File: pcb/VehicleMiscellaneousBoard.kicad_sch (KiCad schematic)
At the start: 13 parts, among them J2 Conn_02x05_Top_Bottom, J4 B8B-XH-A, U1 OpenMV H7+, U2 Seeed_Studio_XIAO-ESP32-S3-Se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

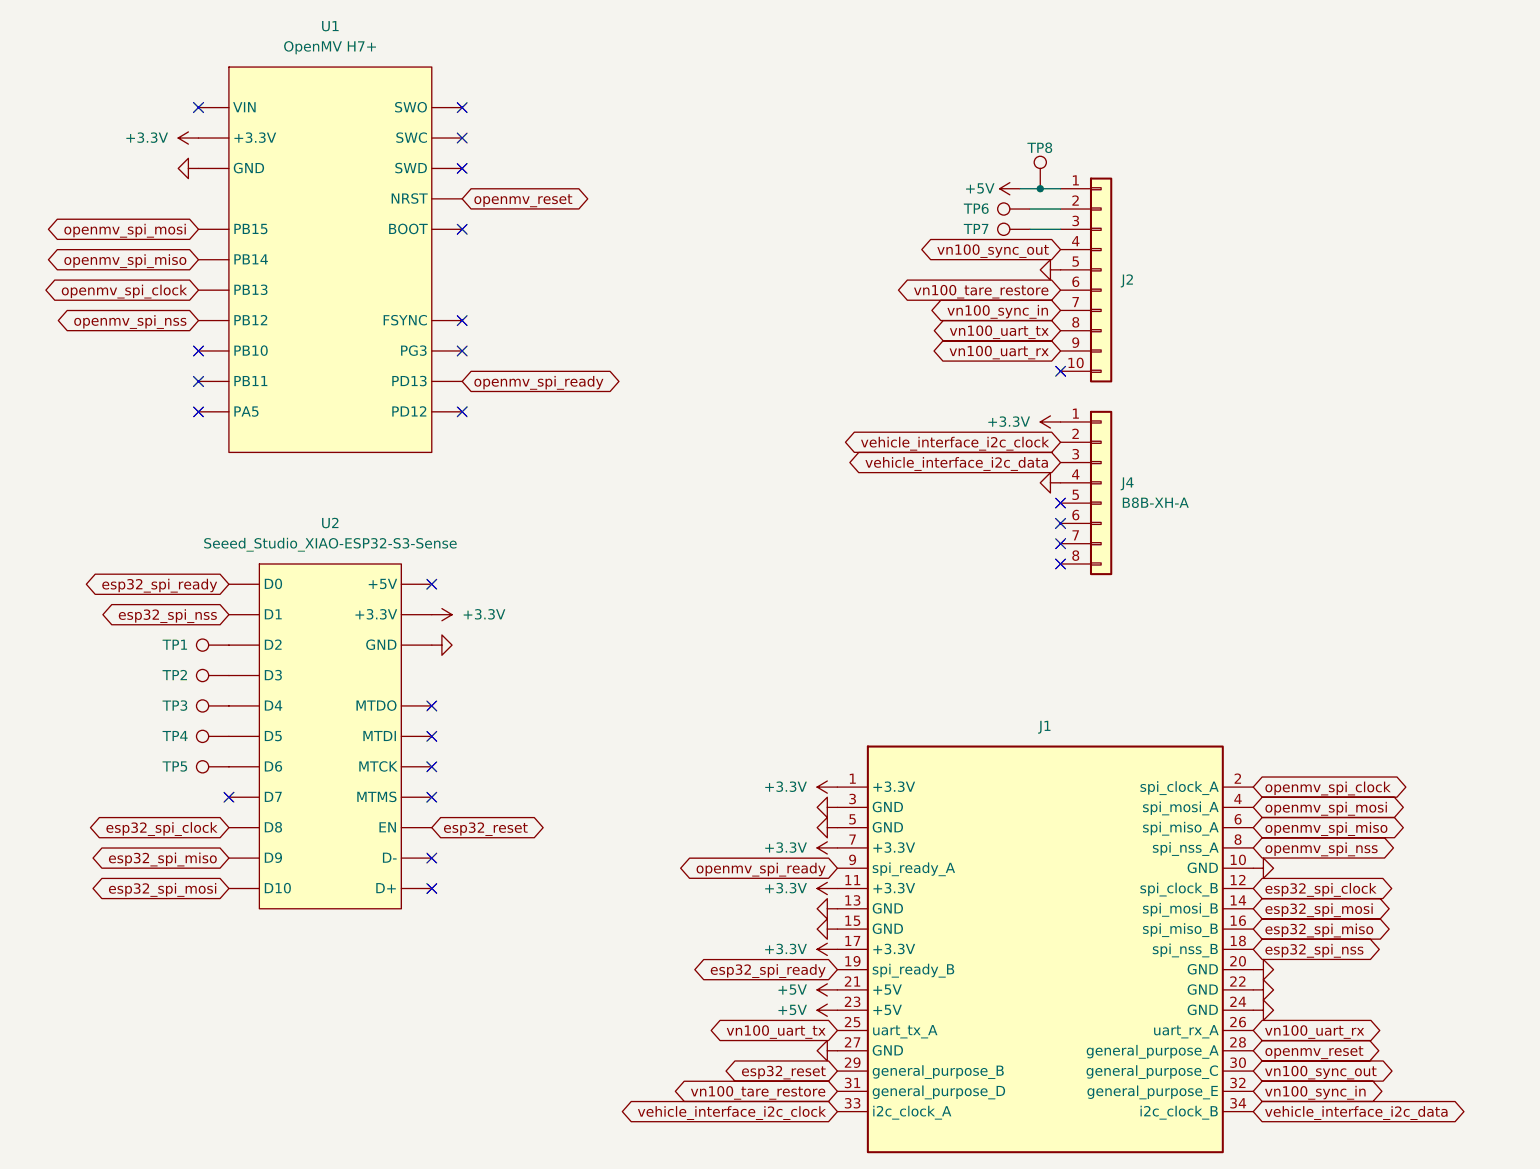
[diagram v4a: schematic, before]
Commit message: Deprecated ESP32 SPI pins for `VehicleFlightComputer` and `VehicleMiscellaneousBoard`.
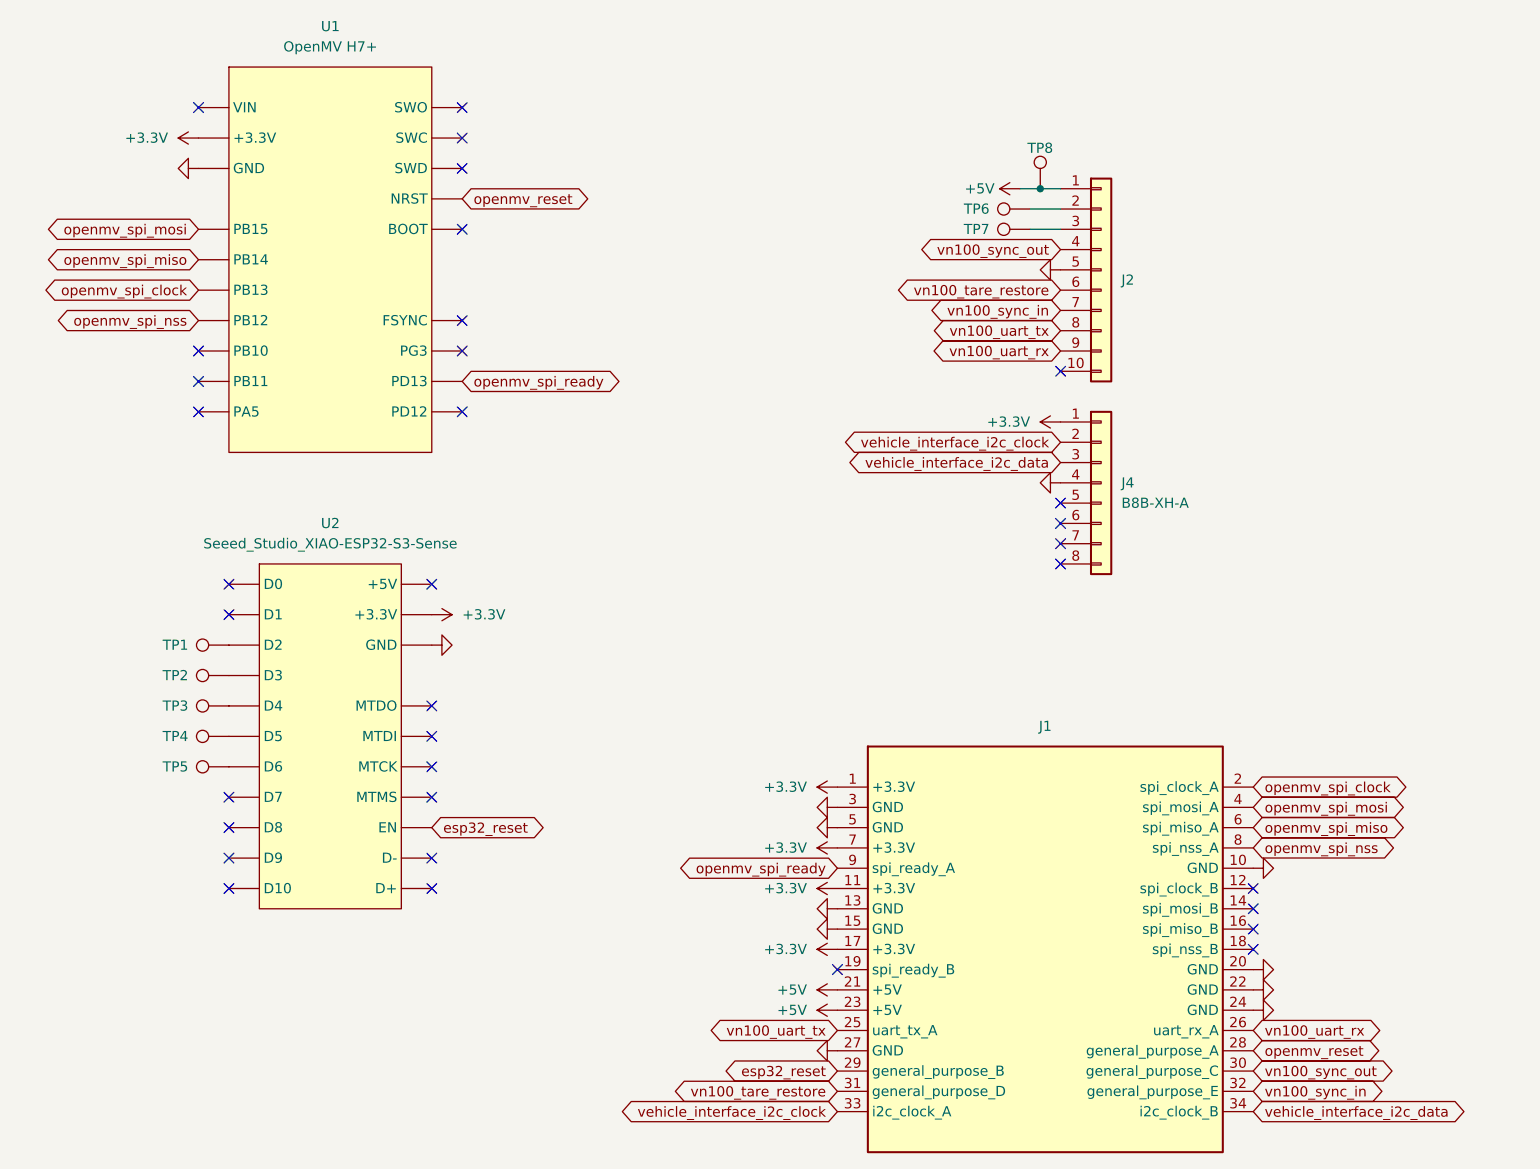
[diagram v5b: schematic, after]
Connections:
- net esp32_spi_clock: no longer names the net of J1.12 (spi_clock_B)
- net esp32_spi_clock: no longer U2.D8
- net esp32_spi_miso: no longer names the net of J1.16 (spi_miso_B)
- net esp32_spi_miso: no longer U2.D9
- net esp32_spi_mosi: no longer names the net of J1.14 (spi_mosi_B)
- net esp32_spi_mosi: no longer U2.D10
- net esp32_spi_nss: no longer names the net of J1.18 (spi_nss_B)
- net esp32_spi_nss: no longer U2.D1
- net esp32_spi_ready: no longer names the net of J1.19 (spi_ready_B)
- net esp32_spi_ready: no longer U2.D0
- no-connect marks 24 -> 34
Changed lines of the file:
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@@
+	)
+	(no_connect
+		(at 224.79 158.75)
 	)
 	(no_connect
@@
 	)
 	(no_connect
+		(at 96.52 115.57)
+	)
+	(no_connect
 		(at 125.73 82.55)
 	)
@@
 	)
 	(no_connect
+		(at 96.52 119.38)
+	)
+	(no_connect
 		(at 125.73 86.36)
 	)
@@
 	)
 	(no_connect
+		(at 96.52 149.86)
+	)
+	(no_connect
+		(at 96.52 153.67)
+	)
+	(no_connect
 		(at 121.92 153.67)
 	)
@@
 	)
 	(no_connect
+		(at 224.79 161.29)
+	)
+	(no_connect
 		(at 200.66 107.95)
 	)
@@
 	)
 	(no_connect
+		(at 172.72 163.83)
+	)
+	(no_connect
 		(at 121.92 115.57)
 	)
@@
 	)
 	(no_connect
+		(at 224.79 156.21)
+	)
+	(no_connect
 		(at 92.71 90.17)
 	)
 	(no_connect
 		(at 125.73 59.69)
+	)
+	(no_connect
+		(at 96.52 146.05)
+	)
+	(no_connect
+		(at 224.79 153.67)
 	)
 	(no_connect
@@
 		)
 	)
-	(global_label "esp32_spi_clock"
-		(shape bidirectional)
-		(at 96.52 146.05 180)
-		(fields_autoplaced yes)
-		(effects
-			(font
-				(size 1.27 1.27)
-			)
-			(justify right)
-		)
-		(property "Intersheetrefs" "${INTERSHEET_REFS}"
-			(at 77.0022 146.05 0)
-			(effects
-				(font
-					(size 1.27 1.27)
-				)
-				(justify right)
-				(hide yes)
-			)
-		)
-	)
 	(global_label "vn100_uart_rx"
 		(shape bidirectional)
@@
 		)
 	)
-	(global_label "esp32_spi_nss"
-		(shape bidirectional)
-		(at 224.79 161.29 0)
-		(fields_autoplaced yes)
-		(effects
-			(font
-				(size 1.27 1.27)
-			)
-			(justify left)
-		)
-		(property "Intersheetrefs" "${INTERSHEET_REFS}"
-			(at 242.4935 161.29 0)
-			(effects
-				(font
-					(size 1.27 1.27)
-				)
-				(justify left)
-				(hide yes)
-			)
-		)
-	)
 	(global_label "vn100_sync_in"
 		(shape bidirectional)
@@
 		)
 	)
-	(global_label "esp32_spi_ready"
-		(shape bidirectional)
-		(at 96.52 115.57 180)
-		(fields_autoplaced yes)
-		(effects
-			(font
-				(size 1.27 1.27)
-			)
-			(justify right)
-		)
-		(property "Intersheetrefs" "${INTERSHEET_REFS}"
-			(at 76.8813 115.57 0)
-			(effects
-				(font
-					(size 1.27 1.27)
-				)
-				(justify right)
-				(hide yes)
-			)
-		)
-	)
 	(global_label "vn100_uart_tx"
 		(shape bidirectional)
@@
 		)
 	)
-	(global_label "esp32_spi_miso"
-		(shape bidirectional)
-		(at 224.79 158.75 0)
-		(fields_autoplaced yes)
-		(effects
-			(font
-				(size 1.27 1.27)
-			)
-			(justify left)
-		)
-		(property "Intersheetrefs" "${INTERSHEET_REFS}"
-			(at 243.7635 158.75 0)
-			(effects
-				(font
-					(size 1.27 1.27)
-				)
-				(justify left)
-				(hide yes)
-			)
-		)
-	)
 	(global_label "openmv_spi_clock"
 		(shape bidirectional)
@@
 		)
 	)
-	(global_label "esp32_spi_mosi"
-		(shape bidirectional)
-		(at 96.52 153.67 180)
-		(fields_autoplaced yes)
-		(effects
-			(font
-				(size 1.27 1.27)
-			)
-			(justify right)
-		)
-		(property "Intersheetrefs" "${INTERSHEET_REFS}"
-			(at 77.5465 153.67 0)
-			(effects
-				(font
-					(size 1.27 1.27)
-				)
-				(justify right)
-				(hide yes)
-			)
-		)
-	)
 	(global_label "esp32_reset"
 		(shape bidirectional)
@@
 		)
 	)
-	(global_label "esp32_spi_mosi"
-		(shape bidirectional)
-		(at 224.79 156.21 0)
-		(fields_autoplaced yes)
-		(effects
-			(font
-				(size 1.27 1.27)
-			)
-			(justify left)
-		)
-		(property "Intersheetrefs" "${INTERSHEET_REFS}"
-			(at 243.7635 156.21 0)
-			(effects
-				(font
-					(size 1.27 1.27)
-				)
-				(justify left)
-				(hide yes)
-			)
-		)
-	)
-	(global_label "esp32_spi_miso"
-		(shape bidirectional)
-		(at 96.52 149.86 180)
-		(fields_autoplaced yes)
-		(effects
-			(font
-				(size 1.27 1.27)
-			)
-			(justify right)
-		)
-		(property "Intersheetrefs" "${INTERSHEET_REFS}"
-			(at 77.5465 149.86 0)
-			(effects
-				(font
-					(size 1.27 1.27)
-				)
-				(justify right)
-				(hide yes)
-			)
-		)
-	)
-	(global_label "esp32_spi_clock"
-		(shape bidirectional)
-		(at 224.79 153.67 0)
-		(fields_autoplaced yes)
-		(effects
-			(font
-				(size 1.27 1.27)
-			)
-			(justify left)
-		)
-		(property "Intersheetrefs" "${INTERSHEET_REFS}"
-			(at 244.3078 153.67 0)
-			(effects
-				(font
-					(size 1.27 1.27)
-				)
-				(justify left)
-				(hide yes)
-			)
-		)
-	)
 	(global_label "vn100_tare_restore"
 		(shape bidirectional)
@@
 		)
 	)
-	(global_label "esp32_spi_ready"
-		(shape bidirectional)
-		(at 172.72 163.83 180)
-		(fields_autoplaced yes)
-		(effects
-			(font
-				(size 1.27 1.27)
-			)
-			(justify right)
-		)
-		(property "Intersheetrefs" "${INTERSHEET_REFS}"
-			(at 153.0813 163.83 0)
-			(effects
-				(font
-					(size 1.27 1.27)
-				)
-				(justify right)
-				(hide yes)
-			)
-		)
-	)
 	(global_label "vehicle_interface_i2c_clock"
 		(shape bidirectional)
@@
 				(hide yes)
 			)
-		)
-	)
-	(global_label "esp32_spi_nss"
-		(shape bidirectional)
-		(at 96.52 119.38 180)
-		(fields_autoplaced yes)
-		(effects
-			(font
-				(size 1.27 1.27)
-			)
-			(justify right)
-		)
-		(property "Intersheetrefs" "${INTERSHEET_REFS}"
-			(at 78.8165 119.38 0)
-			(effects
-				(font
-					(size 1.27 1.27)
-				)
-				(justify right)
-				(hide yes)
-			)

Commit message: Deprecated `vn100_tare_restore`, `vn100_sync_out`, and `vn100_sync_in` for `VehicleFlightComputer` and `VehicleMiscellaneousBoard`.
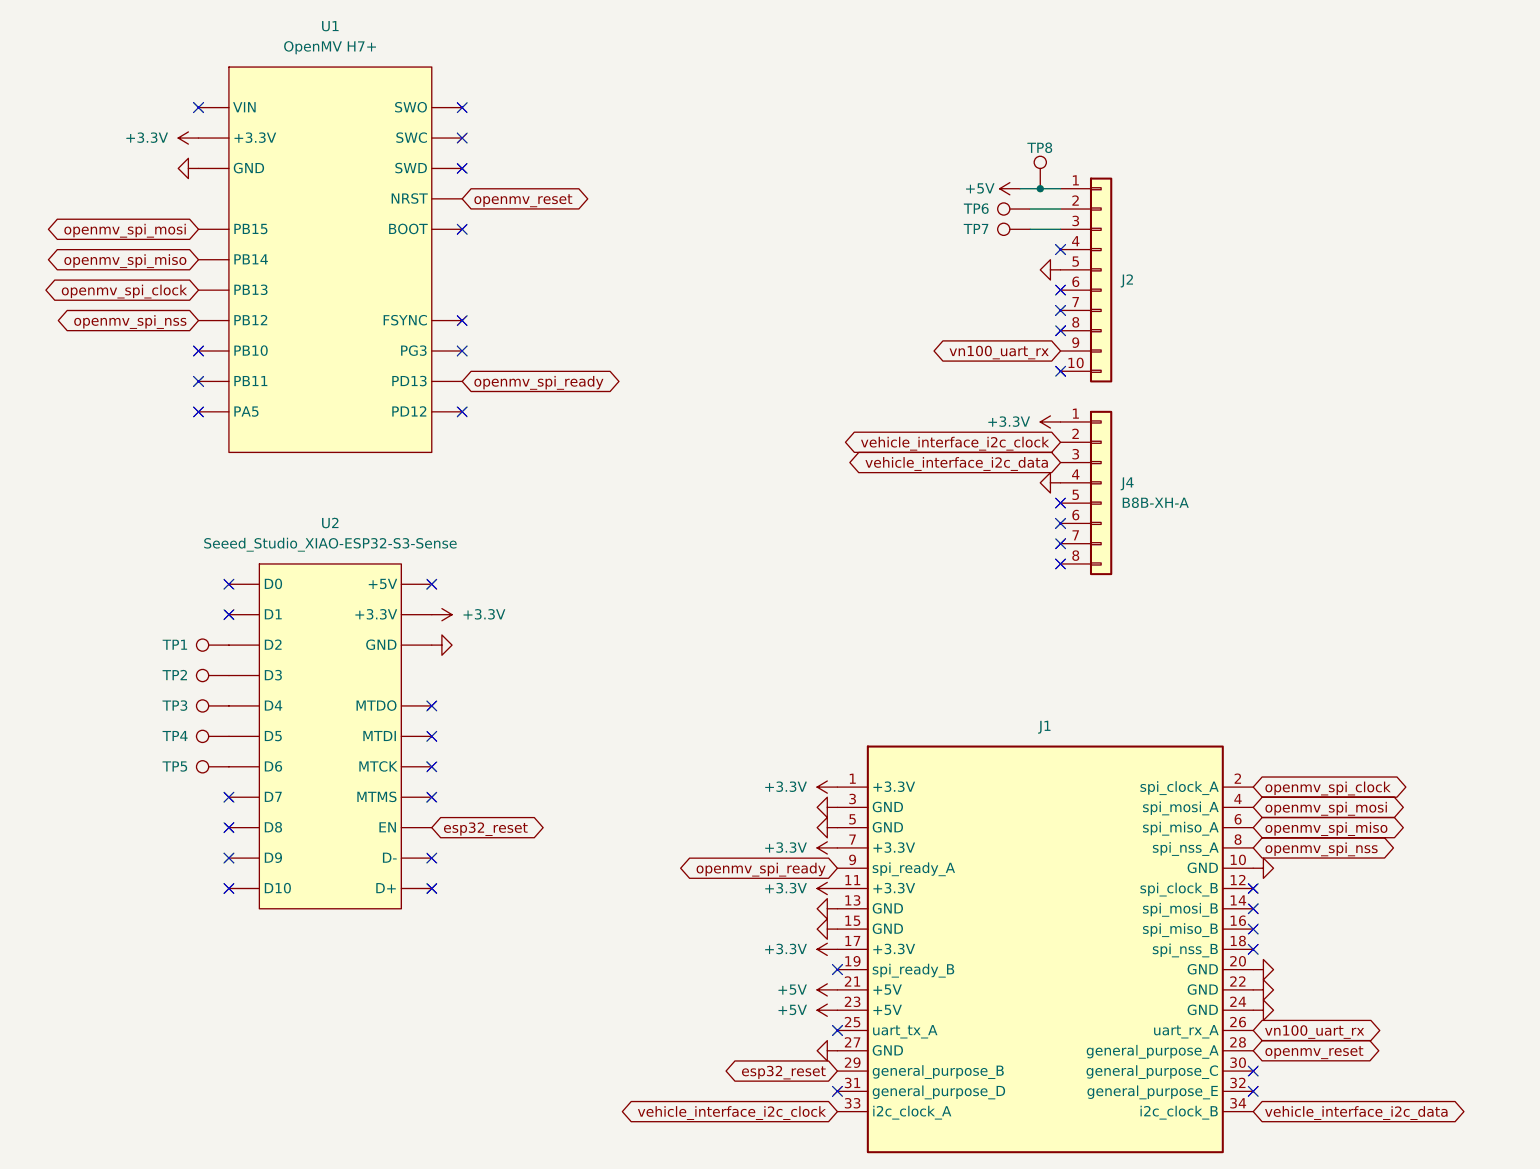
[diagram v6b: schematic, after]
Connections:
- net vn100_sync_in: no longer names the net of J1.32 (general_purpose_E)
- net vn100_sync_in: no longer J2.7 (Pin_7)
- net vn100_sync_out: no longer names the net of J1.30 (general_purpose_C)
- net vn100_sync_out: no longer J2.4 (Pin_4)
- net vn100_tare_restore: no longer names the net of J1.31 (general_purpose_D)
- net vn100_tare_restore: no longer J2.6 (Pin_6)
- net vn100_uart_tx: no longer names the net of J1.25 (uart_tx_A)
- net vn100_uart_tx: no longer J2.8 (Pin_8)
- no-connect marks 34 -> 42
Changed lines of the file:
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@@
+	)
+	(no_connect
+		(at 200.66 78.74)
 	)
 	(no_connect
@@
 	)
 	(no_connect
+		(at 200.66 83.82)
+	)
+	(no_connect
+		(at 200.66 81.28)
+	)
+	(no_connect
 		(at 92.71 55.88)
 	)
@@
 	)
 	(no_connect
+		(at 172.72 171.45)
+	)
+	(no_connect
 		(at 200.66 88.9)
 	)
 	(no_connect
+		(at 224.79 176.53)
+	)
+	(no_connect
 		(at 96.52 149.86)
 	)
@@
 	)
 	(no_connect
+		(at 224.79 179.07)
+	)
+	(no_connect
 		(at 200.66 107.95)
 	)
@@
 	(no_connect
 		(at 96.52 146.05)
+	)
+	(no_connect
+		(at 172.72 179.07)
+	)
+	(no_connect
+		(at 200.66 73.66)
 	)
 	(no_connect
@@
 		)
 	)
-	(global_label "vn100_uart_tx"
-		(shape bidirectional)
-		(at 172.72 171.45 180)
-		(fields_autoplaced yes)
-		(effects
-			(font
-				(size 1.27 1.27)
-			)
-			(justify right)
-		)
-		(property "Intersheetrefs" "${INTERSHEET_REFS}"
-			(at 155.3795 171.45 0)
-			(effects
-				(font
-					(size 1.27 1.27)
-				)
-				(justify right)
-				(hide yes)
-			)
-		)
-	)
 	(global_label "vehicle_interface_i2c_data"
 		(shape bidirectional)
@@
 		)
 	)
-	(global_label "vn100_sync_in"
-		(shape bidirectional)
-		(at 200.66 81.28 180)
-		(fields_autoplaced yes)
-		(effects
-			(font
-				(size 1.27 1.27)
-			)
-			(justify right)
-		)
-		(property "Intersheetrefs" "${INTERSHEET_REFS}"
-			(at 182.8961 81.28 0)
-			(effects
-				(font
-					(size 1.27 1.27)
-				)
-				(justify right)
-				(hide yes)
-			)
-		)
-	)
 	(global_label "openmv_reset"
 		(shape bidirectional)
@@
 		)
 	)
-	(global_label "vn100_uart_tx"
-		(shape bidirectional)
-		(at 200.66 83.82 180)
-		(fields_autoplaced yes)
-		(effects
-			(font
-				(size 1.27 1.27)
-			)
-			(justify right)
-		)
-		(property "Intersheetrefs" "${INTERSHEET_REFS}"
-			(at 183.3195 83.82 0)
-			(effects
-				(font
-					(size 1.27 1.27)
-				)
-				(justify right)
-				(hide yes)
-			)
-		)
-	)
 	(global_label "esp32_reset"
 		(shape bidirectional)
@@
 		)
 	)
-	(global_label "vn100_tare_restore"
-		(shape bidirectional)
-		(at 200.66 78.74 180)
-		(fields_autoplaced yes)
-		(effects
-			(font
-				(size 1.27 1.27)
-			)
-			(justify right)
-		)
-		(property "Intersheetrefs" "${INTERSHEET_REFS}"
-			(at 178.4813 78.74 0)
-			(effects
-				(font
-					(size 1.27 1.27)
-				)
-				(justify right)
-				(hide yes)
-			)
-		)
-	)
 	(global_label "vehicle_interface_i2c_clock"
 		(shape bidirectional)
@@
 		)
 	)
-	(global_label "vn100_sync_in"
-		(shape bidirectional)
-		(at 224.79 179.07 0)
-		(fields_autoplaced yes)
-		(effects
-			(font
-				(size 1.27 1.27)
-			)
-			(justify left)
-		)
-		(property "Intersheetrefs" "${INTERSHEET_REFS}"
-			(at 242.5539 179.07 0)
-			(effects
-				(font
-					(size 1.27 1.27)
-				)
-				(justify left)
-				(hide yes)
-			)
-		)
-	)
-	(global_label "vn100_tare_restore"
-		(shape bidirectional)
-		(at 172.72 179.07 180)
-		(fields_autoplaced yes)
-		(effects
-			(font
-				(size 1.27 1.27)
-			)
-			(justify right)
-		)
-		(property "Intersheetrefs" "${INTERSHEET_REFS}"
-			(at 150.5413 179.07 0)
-			(effects
-				(font
-					(size 1.27 1.27)
-				)
-				(justify right)
-				(hide yes)
-			)
-		)
-	)
 	(global_label "openmv_spi_nss"
 		(shape bidirectional)
@@
 				(hide yes)
 			)
-		)
-	)
-	(global_label "vn100_sync_out"
-		(shape bidirectional)
-		(at 200.66 73.66 180)
-		(fields_autoplaced yes)
-		(effects
-			(font
-				(size 1.27 1.27)
-			)
-			(justify right)
-		)
-		(property "Intersheetrefs" "${INTERSHEET_REFS}"
-			(at 181.6262 73.66 0)
-			(effects
-				(font
-					(size 1.27 1.27)
-				)
-				(justify right)
-				(hide yes)
-			)
-		)
-	)
-	(global_label "vn100_sync_out"
-		(shape bidirectional)
-		(at 224.79 176.53 0)
-		(fields_autoplaced yes)
-		(effects
-			(font
-				(size 1.27 1.27)
-			)
-			(justify left)
-		)
-		(property "Intersheetrefs" "${INTERSHEET_REFS}"
-			(at 243.8238 176.53 0)
-			(effects
-				(font
-					(size 1.27 1.27)
-				)
-				(justify left)
-				(hide yes)
-			)
